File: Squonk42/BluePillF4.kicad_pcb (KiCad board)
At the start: 2 copper layers, 53.3 x 22.9 mm, 167 parts, among them J1 MH20-1, J2 MH20-1, J3 MH_RA4-1, J4 MR07C-06200, J5 U02-BFD3111B0-009, U1 AP2114HA-3.3TRG1, U2 AP2112K3.3-TRG1, U3 STM32F405RGT6, U4 SY6280, Y1 FC-12M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

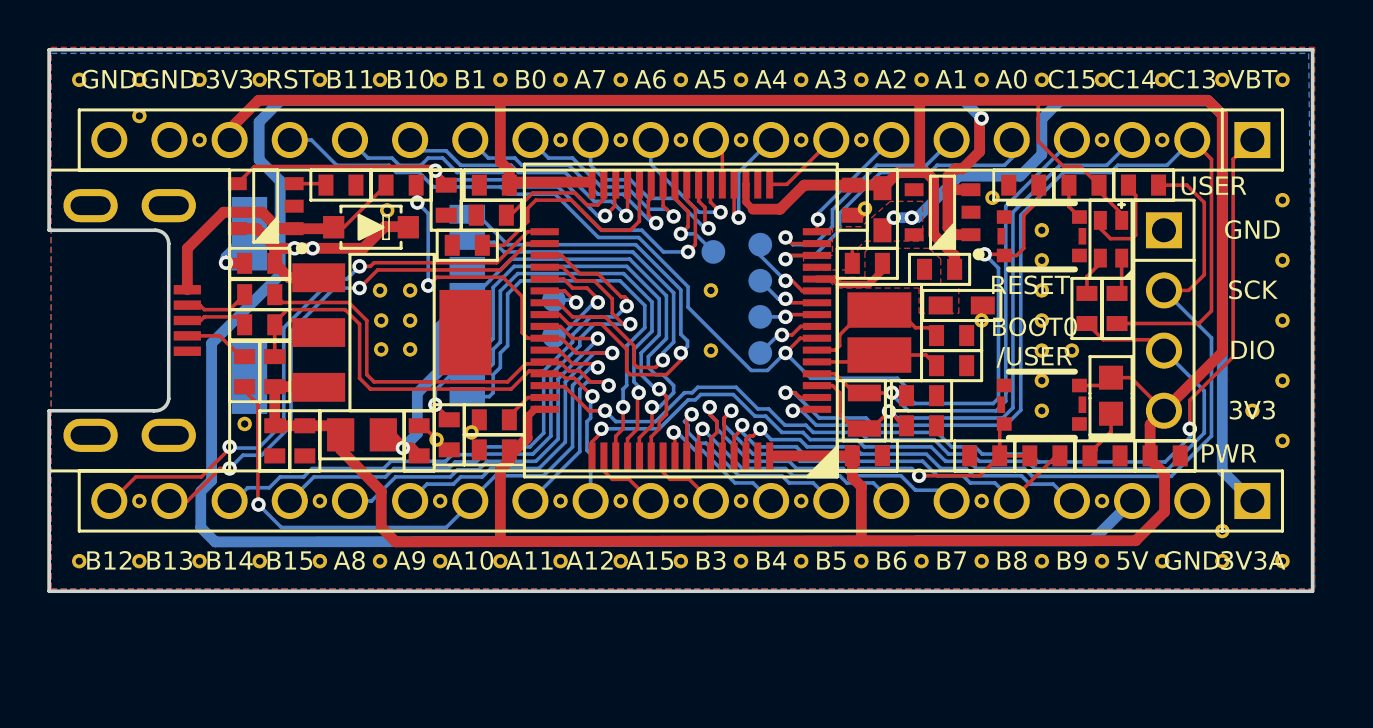
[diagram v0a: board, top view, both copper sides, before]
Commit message: Added LiPo battery charger circuit (option) Put AGND on the analog LDO instead of GND Improved the analog power supply filter Aligned the pads for the PC1-PC7 pins with a 1.27 mm pitch. Now PC0 is used for VBUS_EN instead of PC4 previously
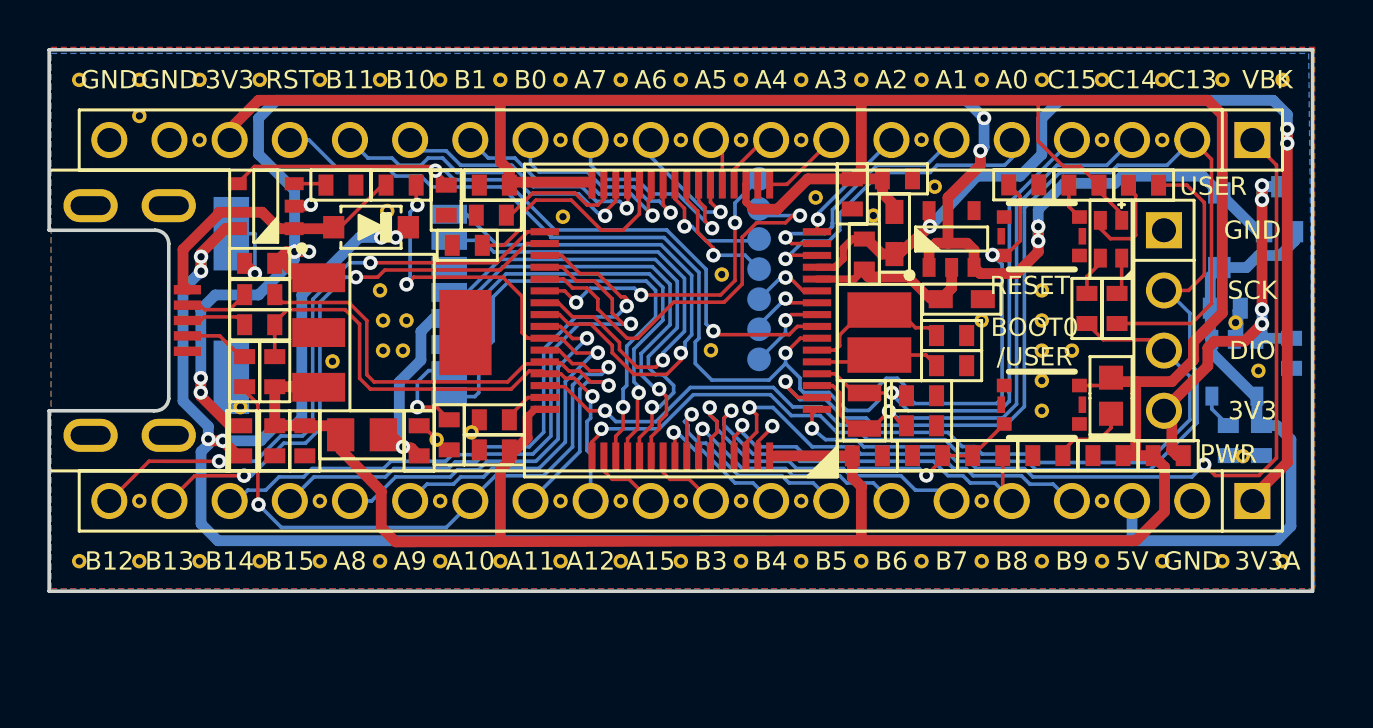
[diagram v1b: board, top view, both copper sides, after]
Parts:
- added C19: 1u, BluePillF4 Lib:C0603, B.Cu at (126.9, 66.1)
- added C20: 1u, BluePillF4 Lib:C0603, B.Cu at (128.2, 62.4)
- added D4: 1N5819HW, BluePillF4 Lib:SOD-123, B.Cu at (125.1, 57.3)
- added PC4: TEST_PAD, BluePillF4 Lib:TEST_PAD, B.Cu at (105.7, 58.9)
- added Q1: IRLML6402, BluePillF4 Lib:SOT323, B.Cu at (127.7, 56.4)
- added R17: 15k, BluePillF4 Lib:R0603, B.Cu at (125.5, 66.1)
- added R18: 10k, BluePillF4 Lib:R0603, B.Cu at (125.4, 60.5)
- added R19: 0R, BluePillF4 Lib:R0603, F.Cu at (83.9, 66.1)
- added R20: 0R, BluePillF4 Lib:R0603, F.Cu at (123.0, 66.8)
- added REF**: VIA_12MIL, BluePillF4 Lib:VIA_12MIL, F.Cu at (87.7, 62.8)
- added REF** (x2): VIA_12MIL, BluePillF4 Lib:VIA_12MIL, F.Cu at (85.2, 55.4)
- added REF**: VIA_12MIL, BluePillF4 Lib:VIA_12MIL, F.Cu at (97.4, 56.7)
- added REF**: VIA_12MIL, BluePillF4 Lib:VIA_12MIL, F.Cu at (108.1, 55.9)
- added REF**: VIA_12MIL, BluePillF4 Lib:VIA_12MIL, F.Cu at (113.1, 55.4)
- added REF**: VIA_12MIL, BluePillF4 Lib:VIA_12MIL, F.Cu at (126.1, 66.8)
- added REF**: VIA_12MIL, BluePillF4 Lib:VIA_12MIL, F.Cu at (126.8, 63.2)
- added REF**: VIA_12MIL, BluePillF4 Lib:VIA_12MIL, F.Cu at (125.8, 61.2)
- added U$4: , BluePillF4 Lib:OPEN_HARDWARE_LOGO, B.Cu at (101.1, 59.8)
- added U5: MCP73812T-420I/OT, BluePillF4 Lib:SOT23-5, B.Cu at (125.8, 63.1)
- moved PC6 10.2 mm to (105.7, 56.4)
- moved PC7 10.1 mm to (105.7, 55.1)
- moved U$6 5.50 mm to (114.8, 61.0)
- moved C1 4.22 mm to (111.5, 55.1), turned to 0 degrees
- moved REF** 2.54 mm to (112.6, 53.4)
- moved C17 2.41 mm to (120.4, 66.8), turned to 0 degrees
- moved R2 2.41 mm to (117.9, 66.8), turned to 0 degrees
- moved R4 2.41 mm to (112.8, 66.8)
- moved R5 2.41 mm to (115.4, 66.8)
- moved PC3 2.30 mm to (105.7, 60.2)
- moved PC2 2.05 mm to (105.7, 61.4)
- moved PC5 2.01 mm to (105.7, 57.6)
- moved PC1 1.79 mm to (105.7, 62.7)
- moved U2 1.19 mm to (113.8, 57.6), turned to 0 degrees
- moved L1 1.13 mm to (111.4, 57.4)
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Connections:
- net /BOOT0 renamed /BluePillF4-1/BOOT0
- net /D1 renamed /BluePillF4-1/D1
- net /D2_B renamed /BluePillF4-1/D2_B
- net /D2_G renamed /BluePillF4-1/D2_G
- net /D2_R renamed /BluePillF4-1/D2_R
- net /DM renamed /BluePillF4-1/DM
- net /DP renamed /BluePillF4-1/DP
- net /ID renamed /BluePillF4-1/ID
- net /ISET renamed /BluePillF4-1/ISET
- net /NRST renamed /BluePillF4-1/NRST
- net /OSCIN renamed /BluePillF4-1/OSCIN
- net /OSCOUT renamed /BluePillF4-1/OSCOUT
- net /PA0 renamed /BluePillF4-1/PA0
- net /PA1 renamed /BluePillF4-1/PA1
- net /PA10 renamed /BluePillF4-1/PA10
- net /PA11 renamed /BluePillF4-1/PA11
- net /PA12 renamed /BluePillF4-1/PA12
- net /PA13 renamed /BluePillF4-1/PA13
- net /PA14 renamed /BluePillF4-1/PA14
- net /PA15 renamed /BluePillF4-1/PA15
- net /PA2 renamed /BluePillF4-1/PA2
- net /PA3 renamed /BluePillF4-1/PA3
- net /PA4 renamed /BluePillF4-1/PA4
- net /PA5 renamed /BluePillF4-1/PA5
- net /PA6 renamed /BluePillF4-1/PA6
- net /PA7 renamed /BluePillF4-1/PA7
- net /PA8 renamed /BluePillF4-1/PA8
- net /PA9 renamed /BluePillF4-1/PA9
- net /PB0 renamed /BluePillF4-1/PB0
- net /PB1 renamed /BluePillF4-1/PB1
- net /PB10 renamed /BluePillF4-1/PB10
- net /PB11 renamed /BluePillF4-1/PB11
- net /PB12 renamed /BluePillF4-1/PB12
- net /PB13 renamed /BluePillF4-1/PB13
- net /PB14 renamed /BluePillF4-1/PB14
- net /PB15 renamed /BluePillF4-1/PB15
- net /PB2 renamed /BluePillF4-1/PB2
- net /PB3 renamed /BluePillF4-1/PB3
- net /PB4 renamed /BluePillF4-1/PB4
- net /PB5 renamed /BluePillF4-1/PB5
- net /PB6 renamed /BluePillF4-1/PB6
- net /PB7 renamed /BluePillF4-1/PB7
- net /PB8 renamed /BluePillF4-1/PB8
- net /PB9 renamed /BluePillF4-1/PB9
- net /PC1 renamed /BluePillF4-1/PC1
- net /PC13 renamed /BluePillF4-1/PC13
- net /PC14 renamed /BluePillF4-1/PC14
- net /PC15 renamed /BluePillF4-1/PC15
- net /PC2 renamed /BluePillF4-1/PC2
- net /PC3 renamed /BluePillF4-1/PC3
- net /PC5 renamed /BluePillF4-1/PC5
- net /PC6 renamed /BluePillF4-1/PC6
- net /PC7 renamed /BluePillF4-1/PC7
- net /R6 renamed /BluePillF4-1/R6
- net /SDIO_CK renamed /BluePillF4-1/SDIO_CK
- net /SDIO_CMD renamed /BluePillF4-1/SDIO_CMD
- net /SDIO_D0 renamed /BluePillF4-1/SDIO_D0
- net /SDIO_D1 renamed /BluePillF4-1/SDIO_D1
- net /SDIO_D2 renamed /BluePillF4-1/SDIO_D2
- net /SDIO_D3 renamed /BluePillF4-1/SDIO_D3
- net /SDIO_VDD renamed /BluePillF4-1/SDIO_VDD
- net /VBAT renamed /BluePillF4-1/VBK
- net /VBUS renamed /BluePillF4-1/VBUS
- net /VCAP_1 renamed /BluePillF4-1/VCAP_1
- net /VCAP_2 renamed /BluePillF4-1/VCAP_2
- C1 pad 2: AGND -> GND
- C6 pad 1: +5V -> +VIN
- J3 pad 4: +3V3 -> +VBAT
- R7 pad 1: /VBUS_EN -> /BluePillF4-1/VBUS_EN
- U1 pad 1: +5V -> +VIN
- U2 pad 1: +5V -> +VIN
- U2 pad 2: GND -> AGND
- U2 pad 3: +5V -> +VIN
- U3 pad 24: /VBUS_EN -> /BluePillF4-1/PC4
- U3 pad 8: /PC0 -> /BluePillF4-1/VBUS_EN
- U4 pad 4: /VBUS_EN -> /BluePillF4-1/VBUS_EN
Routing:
- net +VIN: track 0.00 -> 79.1 mm, vias 0 -> 8
- net /BluePillF4-1/VBUS_EN: track 0.00 -> 30.1 mm, vias 0 -> 2
- net /VBUS_EN: track 24.8 -> 0.00 mm, vias 2 -> 0
- net +VBAT: track 0.00 -> 18.0 mm, vias 0 -> 4
- net +5V: track 110.7 -> 97.2 mm, vias 3 -> 6
- net /BluePillF4-1/PC6: track 5.28 -> 17.2 mm
- net /BluePillF4-1/PC7: track 2.51 -> 13.7 mm, vias 1 -> 3
- net +3V3A: track 34.5 -> 42.9 mm, vias 2 -> 3
- net /BluePillF4-1/PC4: track 0.00 -> 5.64 mm, vias 0 -> 1
- net AGND: track 3.40 -> 7.54 mm
- net +3V3: track 155.8 -> 151.8 mm
- net /BluePillF4-1/NRST: track 48.6 -> 52.0 mm
- net GND: track 6.31 -> 9.63 mm, vias 1 -> 3
- net /BluePillF4-1/VBK: track 32.8 -> 36.1 mm
- net /PC0: track 2.86 -> 0.00 mm, vias 1 -> 0
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- removed copper zone on F.Cu, net +3V3A
- removed copper zone on F.Cu, net AGND
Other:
- board text added: "BluePill F4 (c) 2017-2018"
- board text added: "PC4"
- board text added: "VBK"
- board text removed: "BluePill F4 (c) 2017"
- board text removed: "PC0"
- board text removed: "VBT"

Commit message: Fixed silkscreen on PC7 pad
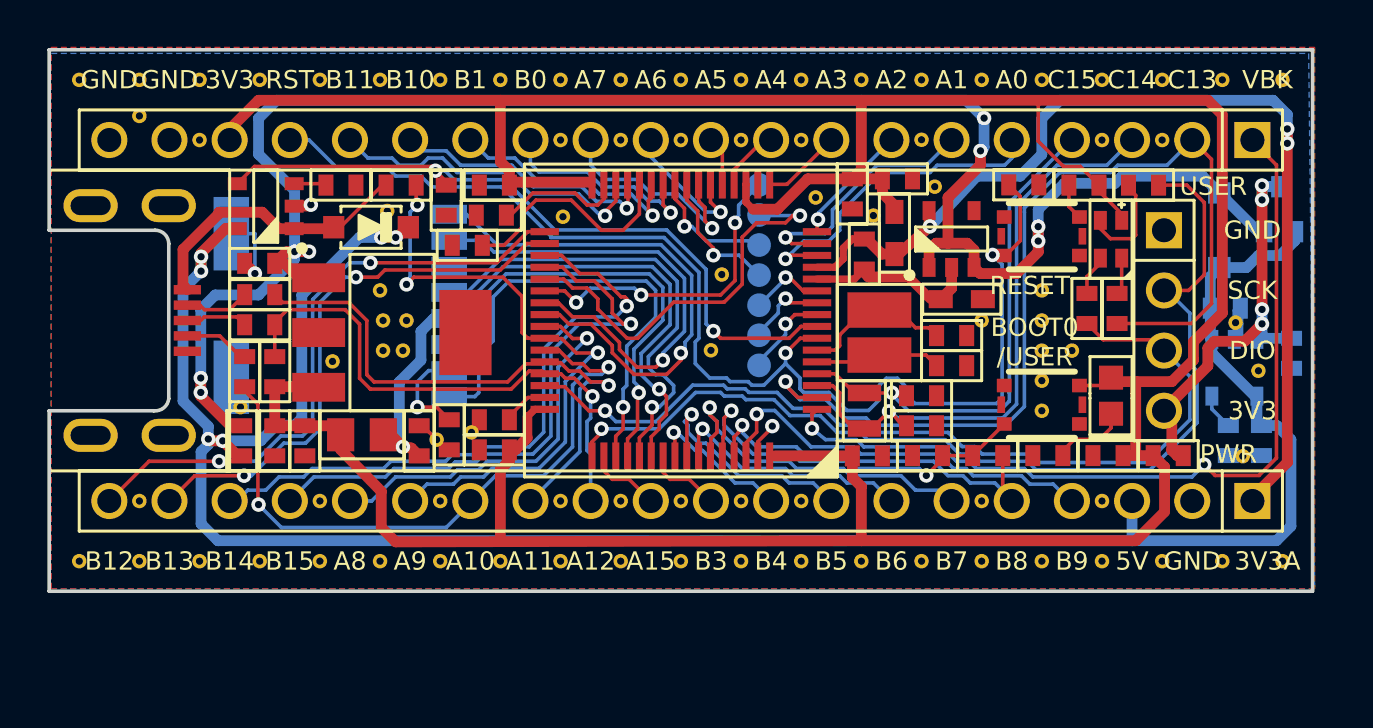
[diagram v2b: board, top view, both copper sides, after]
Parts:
- moved PC0 0.27 mm to (105.7, 62.7)
- moved PC2 0.25 mm to (105.7, 61.7)
- moved PC4 0.25 mm to (105.7, 59.1)
- moved PC1 0.25 mm to (105.7, 63.0)
- moved PC3 0.25 mm to (105.7, 60.4)
- moved PC5 0.25 mm to (105.7, 57.9)
- moved PC6 0.25 mm to (105.7, 56.6)
- moved PC7 0.25 mm to (105.7, 55.3)
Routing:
- net /BluePillF4-1/PB9: track 17.6 -> 16.9 mm

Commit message: Lengthen 0603 resitor and capacitor pads by 5 mils for easier hand soldering Removed 3D model for R8 as it is not mounted for STM32F405 Added Aliexepress column in BOM
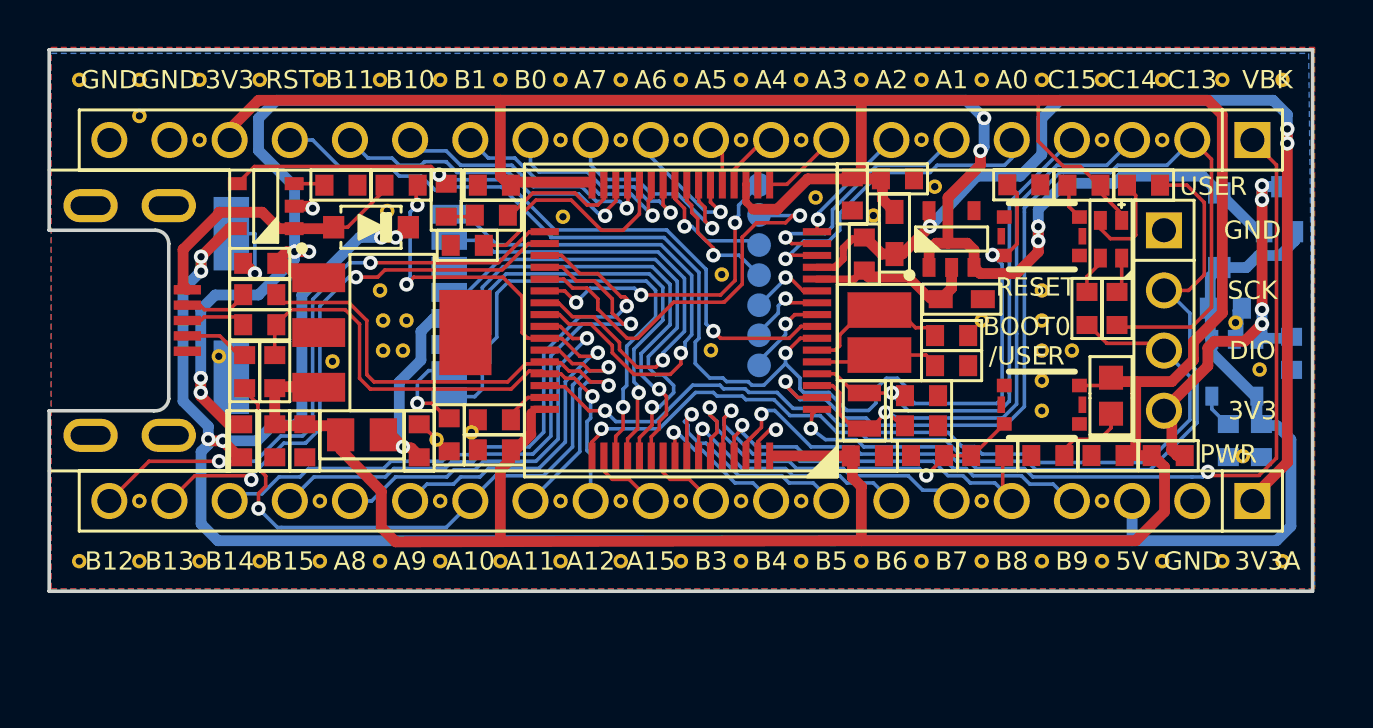
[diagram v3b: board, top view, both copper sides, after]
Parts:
- added REF**: VIA_12MIL, BluePillF4 Lib:VIA_12MIL, F.Cu at (82.9, 62.6)
- moved REF** 0.07 mm to (126.8, 63.1)
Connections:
- REF** pad 1: (no net) -> GND
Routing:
- net GND: track 9.63 -> 11.1 mm
- net /BluePillF4-1/PB9: track 16.9 -> 18.0 mm

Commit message: Replaced the MicroSD Card connector with a Molex 47309-2651 Added voltage sense resistor divider Cleaned up traces
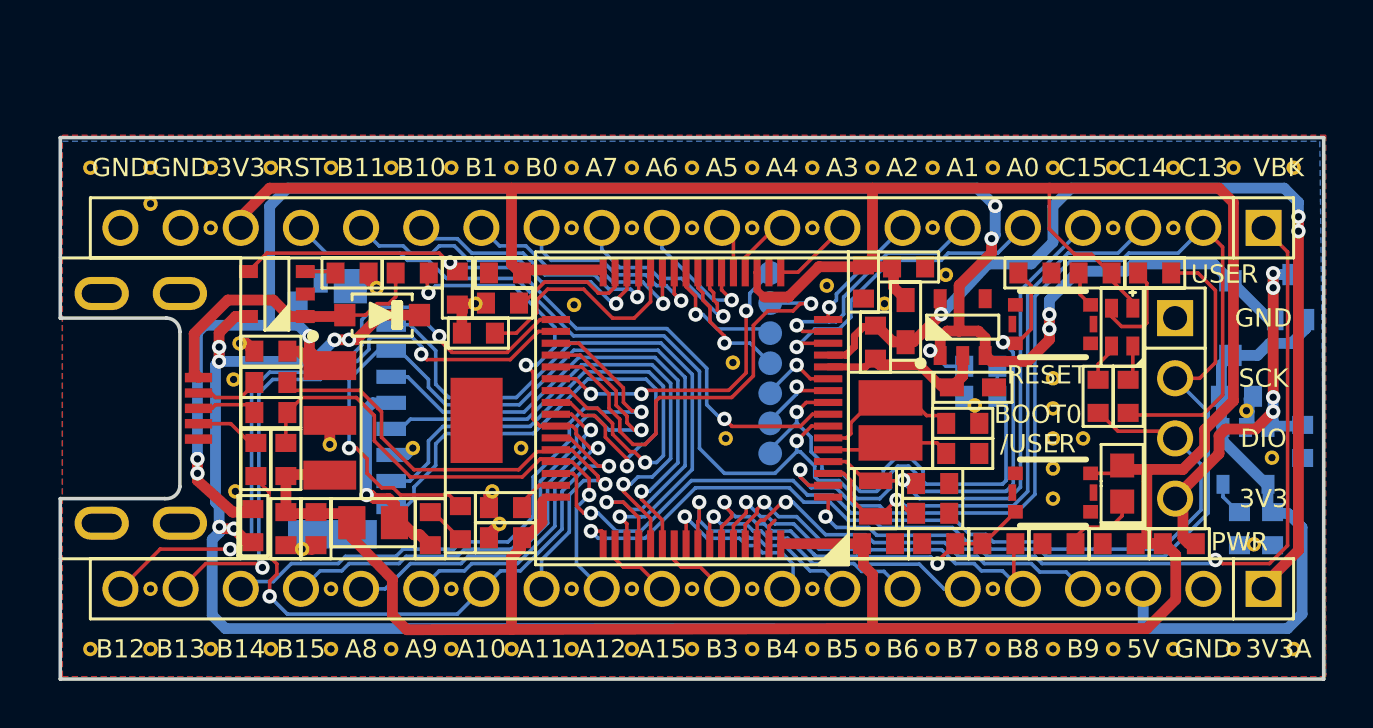
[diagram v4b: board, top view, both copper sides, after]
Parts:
- added R21: 10k, BluePillF4 Lib:R0603, B.Cu at (115.1, 63.0)
- added R22: 10k, BluePillF4 Lib:R0603, B.Cu at (115.1, 64.3)
- added REF**: VIA_12MIL, BluePillF4 Lib:VIA_12MIL, F.Cu at (95.7, 66.4)
- added REF**: VIA_12MIL, BluePillF4 Lib:VIA_12MIL, F.Cu at (94.5, 60.2)
- added REF**: VIA_12MIL, BluePillF4 Lib:VIA_12MIL, F.Cu at (83.5, 63.6)
- added REF**: VIA_12MIL, BluePillF4 Lib:VIA_12MIL, F.Cu at (86.4, 70.7)
- added REF**: VIA_12MIL, BluePillF4 Lib:VIA_12MIL, F.Cu at (83.7, 62.0)
- added REF**: VIA_12MIL, BluePillF4 Lib:VIA_12MIL, F.Cu at (83.5, 66.9)
- J4: value MR07C-06200 -> 47309-2651; footprint BluePillF4 Lib:MR07C-06200 -> BluePillF4 Lib:47309-2651
- moved U$6 7.00 mm to (113.7, 67.9)
- moved U$4 5.40 mm to (99.1, 64.8)
- moved J4 5.27 mm to (90.2, 65.1), turned to 90 degrees
- moved REF** 3.81 mm to (83.3, 66.4)
- moved REF** 3.77 mm to (104.3, 66.0)
- moved L1 3.75 mm to (111.9, 61.1)
- moved L2 3.75 mm to (114.7, 63.9)
- moved R4 3.75 mm to (113.3, 70.5)
- moved C1 3.75 mm to (112.0, 58.8)
- moved C10 3.75 mm to (110.1, 59.4)
- moved C15 3.75 mm to (117.3, 59.1)
- moved C17 3.75 mm to (120.9, 70.5)
- moved C19 3.75 mm to (127.4, 69.8)
- moved C20 3.75 mm to (128.7, 66.2)
- moved C7 3.75 mm to (110.6, 62.0)
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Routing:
- net /BluePillF4-1/PC1: track 3.71 -> 21.0 mm
- net /BluePillF4-1/SDIO_D3: track 24.5 -> 36.4 mm
- net +5V: track 97.3 -> 90.6 mm
- net GND: track 11.1 -> 16.4 mm, vias 3 -> 0
- net /BluePillF4-1/SDIO_D2: track 20.6 -> 25.5 mm
- net +VIN: track 79.1 -> 82.6 mm
- net /BluePillF4-1/PB12: track 26.2 -> 29.0 mm
- net /BluePillF4-1/PB13: track 23.7 -> 26.2 mm
- net /BluePillF4-1/SDIO_D0: track 20.9 -> 23.3 mm
- net /BluePillF4-1/SDIO_CK: track 19.9 -> 21.9 mm
- net /BluePillF4-1/PC6: track 17.1 -> 19.1 mm
- net /BluePillF4-1/PA11: track 24.7 -> 23.0 mm
- net /BluePillF4-1/PA10: track 28.3 -> 26.6 mm
- net /BluePillF4-1/SDIO_CMD: track 20.7 -> 22.2 mm
- net /BluePillF4-1/PB9: track 18.0 -> 16.5 mm
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
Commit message: Corrected truncated measurement values for trace width and clearance
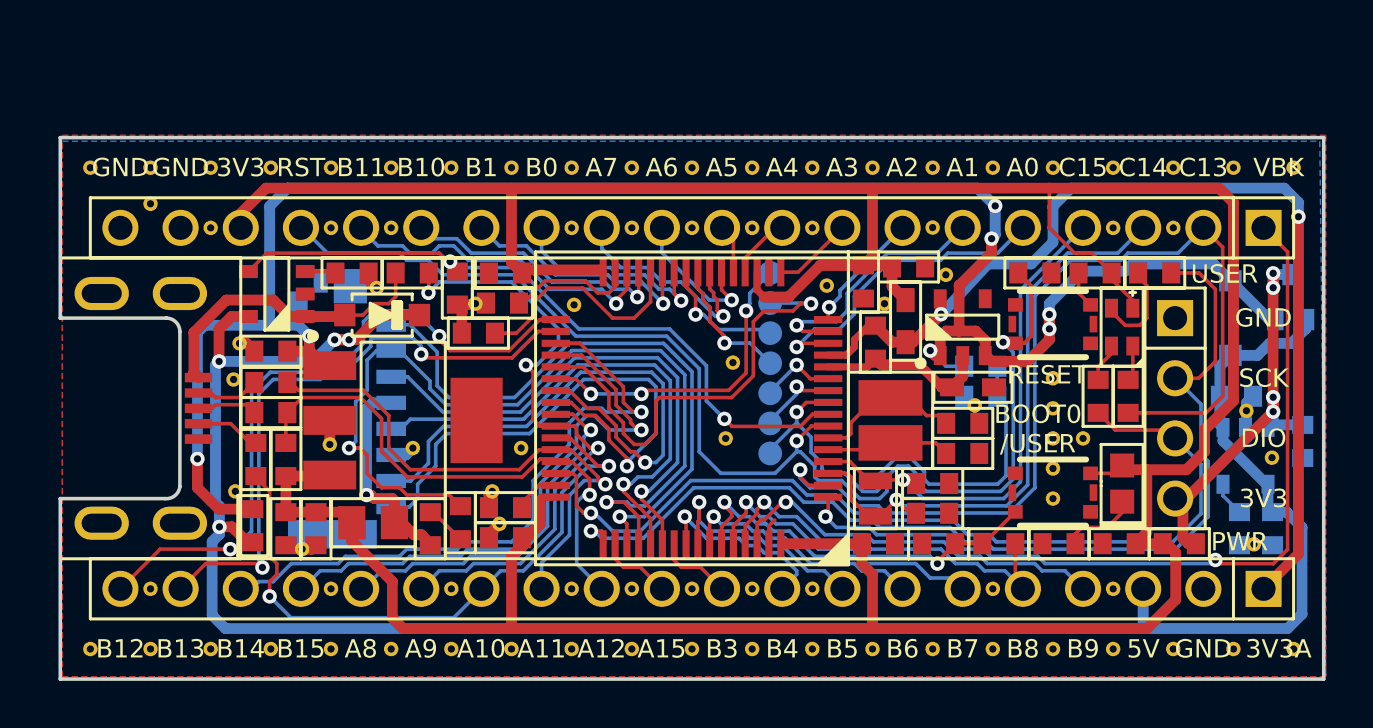
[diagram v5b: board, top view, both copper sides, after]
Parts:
- added REF**: VIA_12MIL, BluePillF4 Lib:VIA_12MIL, F.Cu at (90.2, 57.1)
- added REF**: VIA_12MIL, BluePillF4 Lib:VIA_12MIL, F.Cu at (87.6, 57.1)
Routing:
- net +VBAT: track 18.0 -> 19.6 mm
- net /BluePillF4-1/PB7: track 14.6 -> 13.7 mm
- net GND: track 16.4 -> 15.6 mm
- net +3V3: track 151.8 -> 152.5 mm
- net /BluePillF4-1/SDIO_D3: track 36.4 -> 37.0 mm
- net +3V3A: track 42.9 -> 42.3 mm, vias 3 -> 2
- net /BluePillF4-1/VBUS_EN: track 29.4 -> 29.9 mm
- net +VIN: track 82.6 -> 82.2 mm, vias 8 -> 7
- net +5V: vias 6 -> 4
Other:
- net class Default: clearance 0.1523 -> 0.1524; trace_width 0.1523 -> 0.1524
- net class Power: clearance 0.1523 -> 0.1524; trace_width 0.305 -> 0.3048
- rule trace_clearance: 0.1523 -> 0.1524
- rule trace_min: 0.1523 -> 0.1524
